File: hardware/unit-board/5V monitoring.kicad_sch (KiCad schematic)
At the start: 4 parts

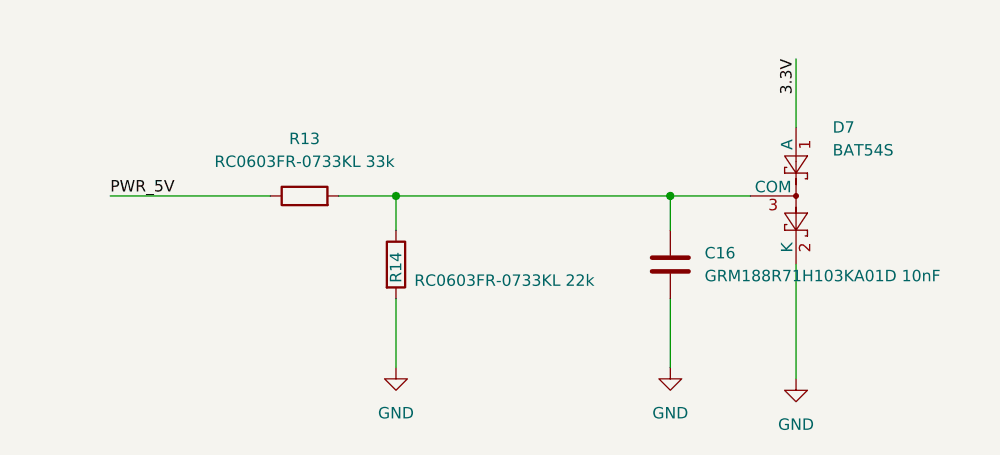
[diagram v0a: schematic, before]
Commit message: fix(hardware): resolve unit board ERC violations
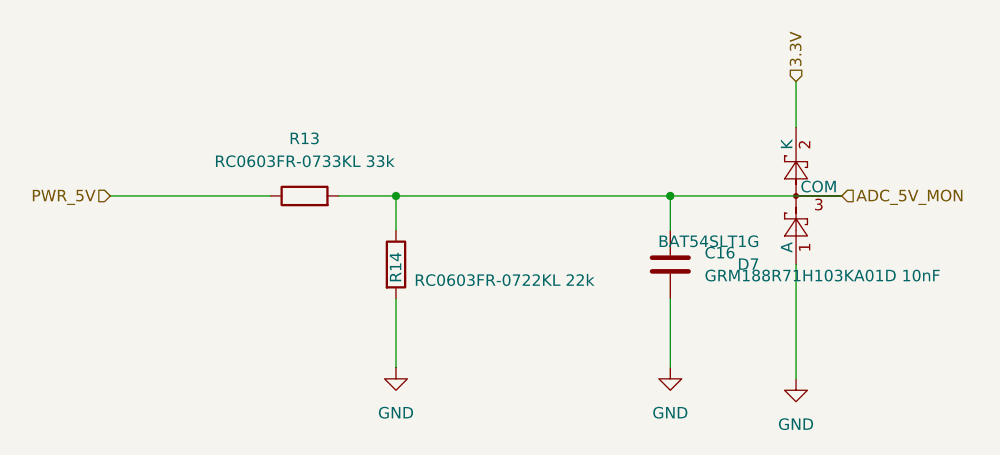
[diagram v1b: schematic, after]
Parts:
- D7: value BAT54S -> BAT54SLT1G
- R14: value RC0603FR-0733KL 22k -> RC0603FR-0722KL 22k
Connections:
- net 3.3V: now also D7.2 (K); no longer D7.1 (A)
- net GND: now also D7.1 (A); no longer D7.2 (K)
- net ADC_5V_MON: now reaches C16.1, D7.3 (COM), R13.2, R14.1
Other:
- moved on the sheet: D7
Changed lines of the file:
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@@
+	(wire
+		(pts
+			(xy 132.08 43.18) (xy 132.08 48.26)
+		)
+		(stroke
+			(width 0)
+			(type default)
+		)
+	)
 	(wire
 		(pts
@@
 	(wire
 		(pts
-			(xy 118.11 55.88) (xy 127 55.88)
+			(xy 118.11 55.88) (xy 137.16 55.88)
 		)
 		(stroke
@@
 	(wire
 		(pts
-			(xy 132.08 40.64) (xy 132.08 48.26)
-		)
-		(stroke
-			(width 0)
-			(type default)
-		)
-	)
-	(wire
-		(pts
 			(xy 118.11 67.31) (xy 118.11 74.93)
 		)
@@
 		)
 	)
-	(label "PWR_5V"
-		(at 55.88 55.88 0)
+	(hierarchical_label "PWR_5V"
+		(shape input)
+		(at 55.88 55.88 180)
 		(effects
 			(font
 				(size 1.27 1.27)
 			)
-			(justify left bottom)
-		)
-	)
-	(label "3.3V"
-		(at 132.08 40.64 270)
+			(justify right)
+		)
+	)
+	(hierarchical_label "ADC_5V_MON"
+		(shape input)
+		(at 137.16 55.88 0)
 		(effects
 			(font
 				(size 1.27 1.27)
 			)
-			(justify right bottom)
+			(justify left)
+		)
+	)
+	(hierarchical_label "3.3V"
+		(shape input)
+		(at 132.08 43.18 90)
+		(effects
+			(font
+				(size 1.27 1.27)
+			)
+			(justify left)
 		)
 	)
@@
 			)
 		)
-		(property "Value" "RC0603FR-0733KL 22k"
+		(property "Value" "RC0603FR-0722KL 22k"
 			(at 89.662 65.278 0)
 			(show_name no)
@@
 	(symbol
 		(lib_id "Diode:BAT54S")
-		(at 132.08 55.88 270)
+		(at 132.08 55.88 90)
 		(unit 1)
 		(body_style 1)
@@
 		(dnp no)
 		(property "Reference" "D7"
-			(at 136.144 48.26 90)
-			(show_name no)
-			(do_not_autoplace no)
-			(effects
-				(font
-					(size 1.27 1.27)
-				)
-				(justify left)
-			)
-		)
-		(property "Value" "BAT54S"
-			(at 136.144 50.8 90)
+			(at 128.016 63.5 90)
+			(show_name no)
+			(do_not_autoplace no)
+			(effects
+				(font
+					(size 1.27 1.27)
+				)
+				(justify left)
+			)
+		)
+		(property "Value" "BAT54SLT1G"
+			(at 128.016 60.96 90)
 			(show_name no)
 			(do_not_autoplace no)
@@
 		)
 		(property "Footprint" "Package_TO_SOT_SMD:SOT-23"
-			(at 135.255 57.785 0)
+			(at 128.905 53.975 0)
 			(hide yes)
 			(show_name no)
@@
 		)
 		(property "Datasheet" "https://www.diodes.com/assets/Datasheets/ds11005.pdf"
-			(at 132.08 52.832 0)
-			(hide yes)
-			(show_name no)
+			(at 132.08 58.928 0)
+			(hide yes)
+			(show_name no)
